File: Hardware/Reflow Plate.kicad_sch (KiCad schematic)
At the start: 30 parts, among them J3 Conn_02x03_Odd_Even, J4 Conn_02x03_Odd_Even, J5 Conn_02x03_Odd_Even, J6 Conn_02x03_Odd_Even, J7 Conn_01x04_Pin, Q2 Q_NMOS_GDS, SW2 SW_Push, SW3 SW_Push, SW4 SW_Push, U3 STM32F103CBTx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

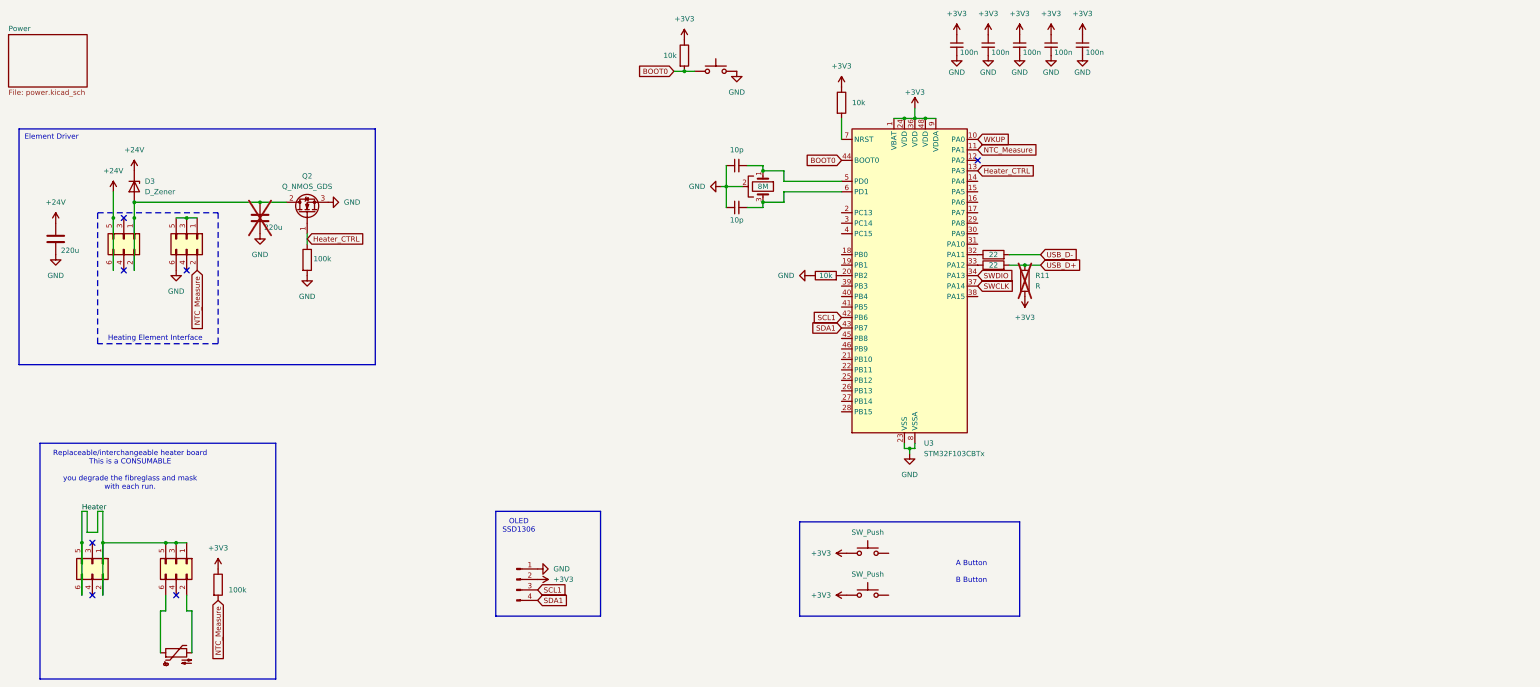
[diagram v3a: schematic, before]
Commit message: Rev 'b'. Having this produced. Added some voltage monitors. cleaned up traces. Moved i2c lines to i2c2. forgot to add pull-ups. the ones in the display should work though.
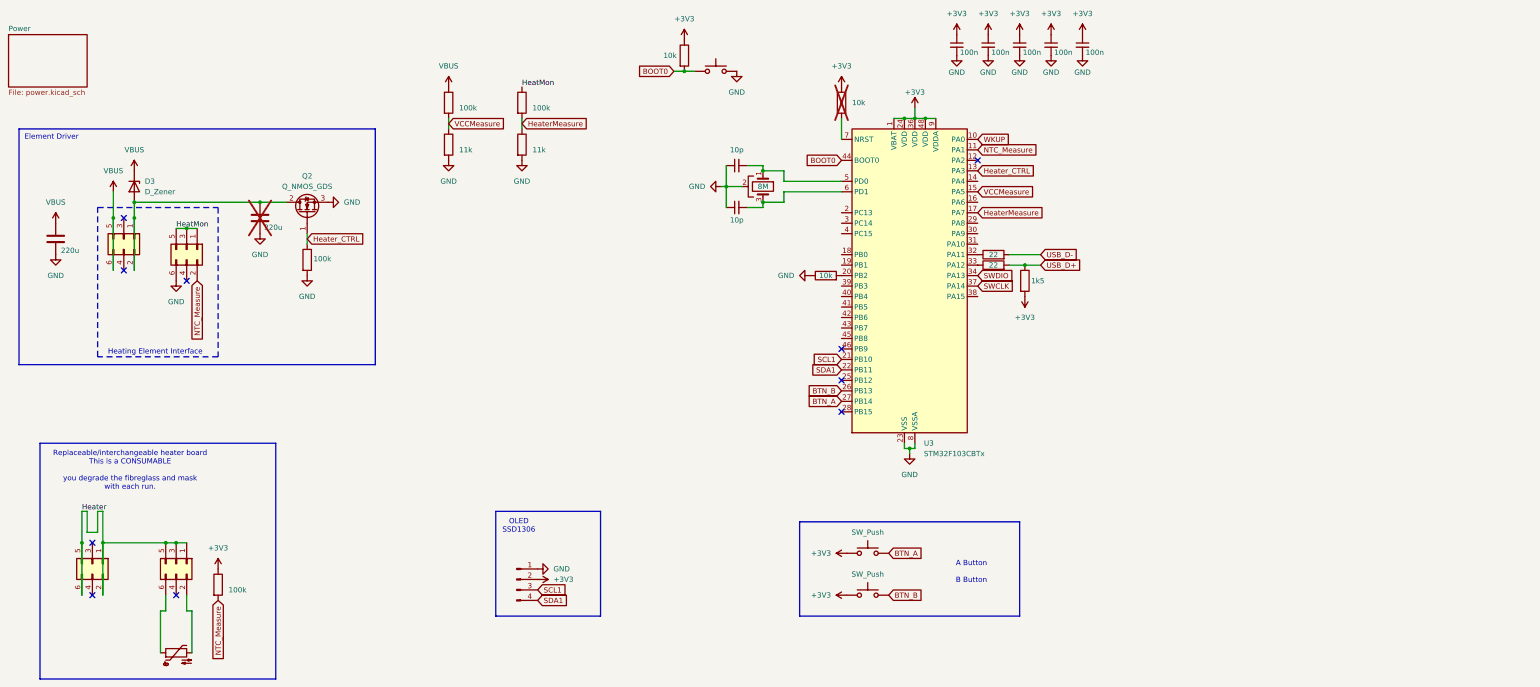
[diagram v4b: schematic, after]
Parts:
- added R12, R14: 100k, Resistor_SMD:R_0402_1005Metric, symbol Device:R
- added R13, R15: 11k, Resistor_SMD:R_0402_1005Metric, symbol Device:R
- R11: value R -> 1k5; now fitted
- R8: now not fitted; now left out of the parts list
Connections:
- net GND: now also R13.2, R15.2
- net SCL1: now also U3.21 (PB10); no longer U3.42 (PB6)
- net SDA1: now also U3.22 (PB11); no longer U3.43 (PB7)
- net HeatMon: now reaches J6.1 (Pin_1), J6.3 (Pin_3), J6.5 (Pin_5)
- net HeatMon: now also R14.1
- net BTN_A: now reaches SW3.2
- net BTN_A: now also U3.27 (PB14)
- net VCCMeasure: now reaches U3.15 (PA5)
- net VCCMeasure: now also R12.2, R13.1
- net HeaterMeasure: now reaches U3.17 (PA7)
- net HeaterMeasure: now also R14.2, R15.1
- net BTN_B: now reaches U3.26 (PB13)
- net BTN_B: now also SW4.2
- net +24V renamed VBUS
- net VBUS: now also R12.1
- no-connect marks 7 -> 10

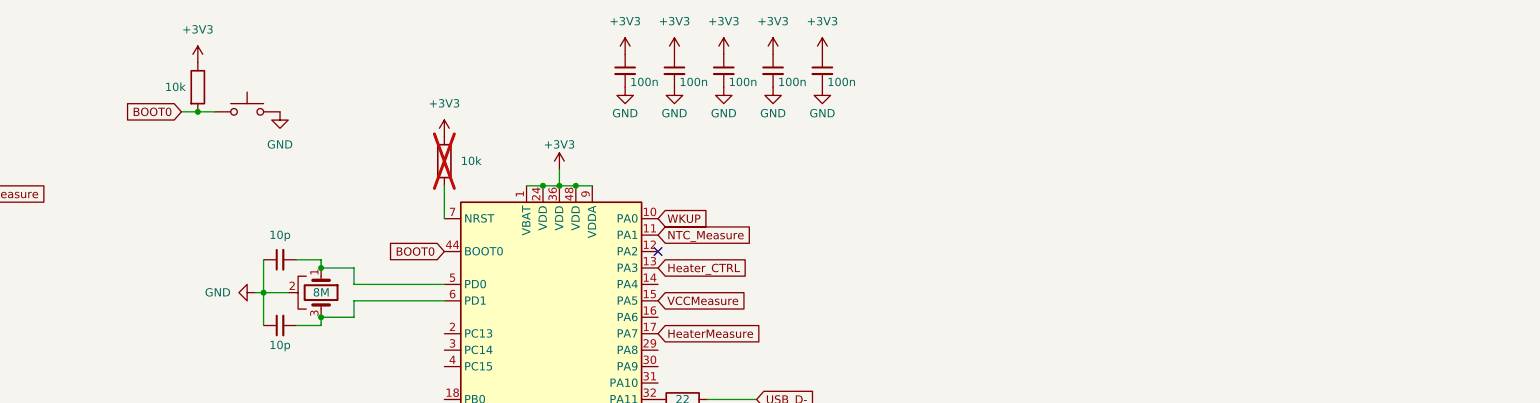
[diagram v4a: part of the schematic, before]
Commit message: Initial Prototype gerbers. Found problems.
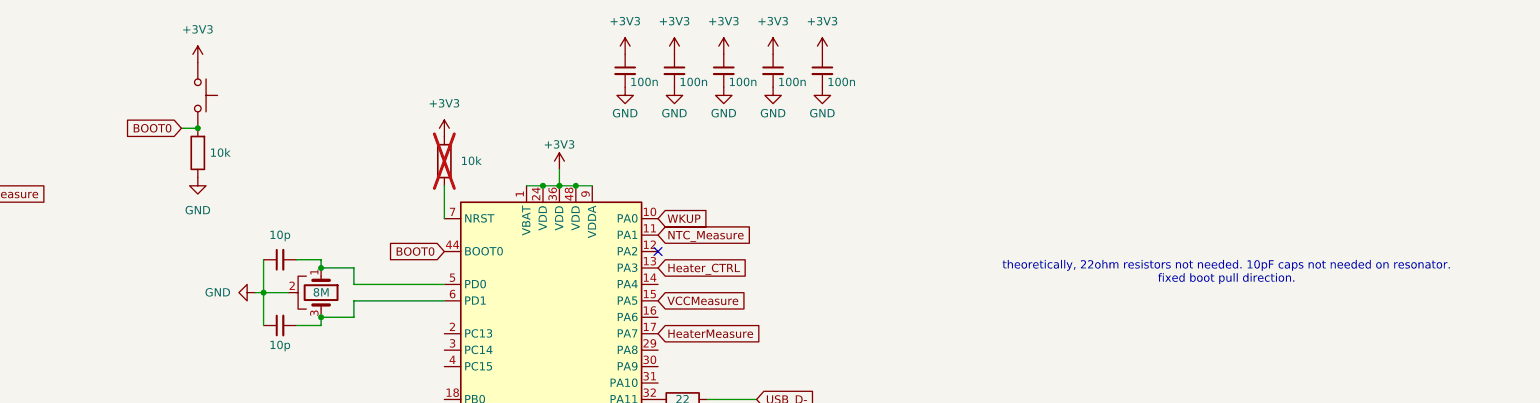
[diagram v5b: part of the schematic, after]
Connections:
- net +3V3: now also SW2.1; no longer R6.1
- net BOOT0: now also SW2.2; no longer SW2.1
- net GND: now also R6.1; no longer SW2.2
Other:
- note added: "theoretically, 22ohm resistors not needed. 10pF caps not needed on resonator. fixed boot pull direction."
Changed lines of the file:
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@@
 	)
 	(junction
+		(at 180.34 30.48)
+		(diameter 0)
+		(color 0 0 0 0)
+	)
+	(junction
 		(at 236.22 39.37)
 		(diameter 0)
@@
 		(color 0 0 0 0)
 	)
-	(junction
-		(at 180.34 27.94)
-		(diameter 0)
-		(color 0 0 0 0)
-	)
 	(no_connect
 		(at 36.83 154.94)
@@
 	(wire
 		(pts
-			(xy 177.8 27.94) (xy 180.34 27.94)
+			(xy 177.8 30.48) (xy 180.34 30.48)
 		)
 		(stroke
@@
 	(wire
 		(pts
-			(xy 180.34 27.94) (xy 182.88 27.94)
-		)
-		(stroke
-			(width 0)
-			(type default)
-		)
-	)
-	(wire
-		(pts
 			(xy 39.37 142.24) (xy 39.37 154.94)
 		)
@@
 		)
 	)
+	(text "theoretically, 22ohm resistors not needed. 10pF caps not needed on resonator.\nfixed boot pull direction.\n"
+		(exclude_from_sim no)
+		(at 339.344 52.832 0)
+		(effects
+			(font
+				(size 1.27 1.27)
+			)
+		)
+	)
 	(text "Replaceable/interchangeable heater board\nThis is a CONSUMABLE\n\nyou degrade the fibreglass and mask\nwith each run."
 		(exclude_from_sim no)
@@
 	(global_label "BOOT0"
 		(shape input)
-		(at 177.8 27.94 180)
+		(at 177.8 30.48 180)
 		(fields_autoplaced yes)
 		(effects
@@
 		)
 		(property "Intersheetrefs" "${INTERSHEET_REFS}"
-			(at 168.7067 27.94 0)
+			(at 168.7067 30.48 0)
 			(effects
 				(font
@@
 	(symbol
 		(lib_id "Device:R")
-		(at 180.34 24.13 0)
+		(at 180.34 34.29 180)
 		(unit 1)
 		(exclude_from_sim no)
@@
 		(dnp no)
 		(property "Reference" "R6"
-			(at 182.88 22.8599 0)
+			(at 177.8 35.5601 0)
 			(effects
 				(font
@@
 		)
 		(property "Value" "10k"
-			(at 175.26 24.13 0)
+			(at 185.42 34.29 0)
 			(effects
 				(font
@@
 		)
 		(property "Footprint" "Resistor_SMD:R_0402_1005Metric"
-			(at 178.562 24.13 90)
+			(at 182.118 34.29 90)
 			(effects
 				(font
@@
 		)
 		(property "Datasheet" "~"
-			(at 180.34 24.13 0)
+			(at 180.34 34.29 0)
 			(effects
 				(font
@@
 		)
 		(property "Description" "Resistor"
-			(at 180.34 24.13 0)
+			(at 180.34 34.29 0)
 			(effects
 				(font
@@
 	(symbol
 		(lib_id "power:GND")
-		(at 193.04 27.94 0)
+		(at 180.34 38.1 0)
 		(unit 1)
 		(exclude_from_sim no)
@@
 		(fields_autoplaced yes)
 		(property "Reference" "#PWR022"
-			(at 193.04 34.29 0)
+			(at 180.34 44.45 0)
 			(effects
 				(font
@@
 		)
 		(property "Value" "GND"
-			(at 193.04 33.02 0)
+			(at 180.34 43.18 0)
 			(effects
 				(font
@@
 		)
 		(property "Footprint" ""
-			(at 193.04 27.94 0)
+			(at 180.34 38.1 0)
 			(effects
 				(font
@@
 		)
 		(property "Datasheet" ""
-			(at 193.04 27.94 0)
+			(at 180.34 38.1 0)
 			(effects
 				(font
@@
 		)
 		(property "Description" "Power symbol creates a global label with name \"GND\" , ground"
-			(at 193.04 27.94 0)
+			(at 180.34 38.1 0)
 			(effects
 				(font
@@
 	(symbol
 		(lib_id "Switch:SW_Push")
-		(at 187.96 27.94 0)
+		(at 180.34 25.4 270)
 		(unit 1)
 		(exclude_from_sim no)
@@
 		(fields_autoplaced yes)
 		(property "Reference" "SW2"
-			(at 187.96 20.32 0)
+			(at 187.96 25.4 0)
 			(effects
 				(font
@@
 		)
 		(property "Value" "SW_Push"
-			(at 187.96 22.86 0)
+			(at 185.42 25.4 0)
 			(effects
 				(font
@@
 		)
 		(property "Footprint" "Button_Switch_SMD:SW_Push_1P1T_XKB_TS-1187A"
-			(at 187.96 22.86 0)
+			(at 185.42 25.4 0)
 			(effects
 				(font
@@
 		)
 		(property "Datasheet" "~"
-			(at 187.96 22.86 0)
+			(at 185.42 25.4 0)
 			(effects
 				(font
@@
 		)
 		(property "Description" "Push button switch, generic, two pins"
-			(at 187.96 27.94 0)
+			(at 180.34 25.4 0)
 			(effects
 				(font
